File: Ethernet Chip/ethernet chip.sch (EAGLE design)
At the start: 32 parts

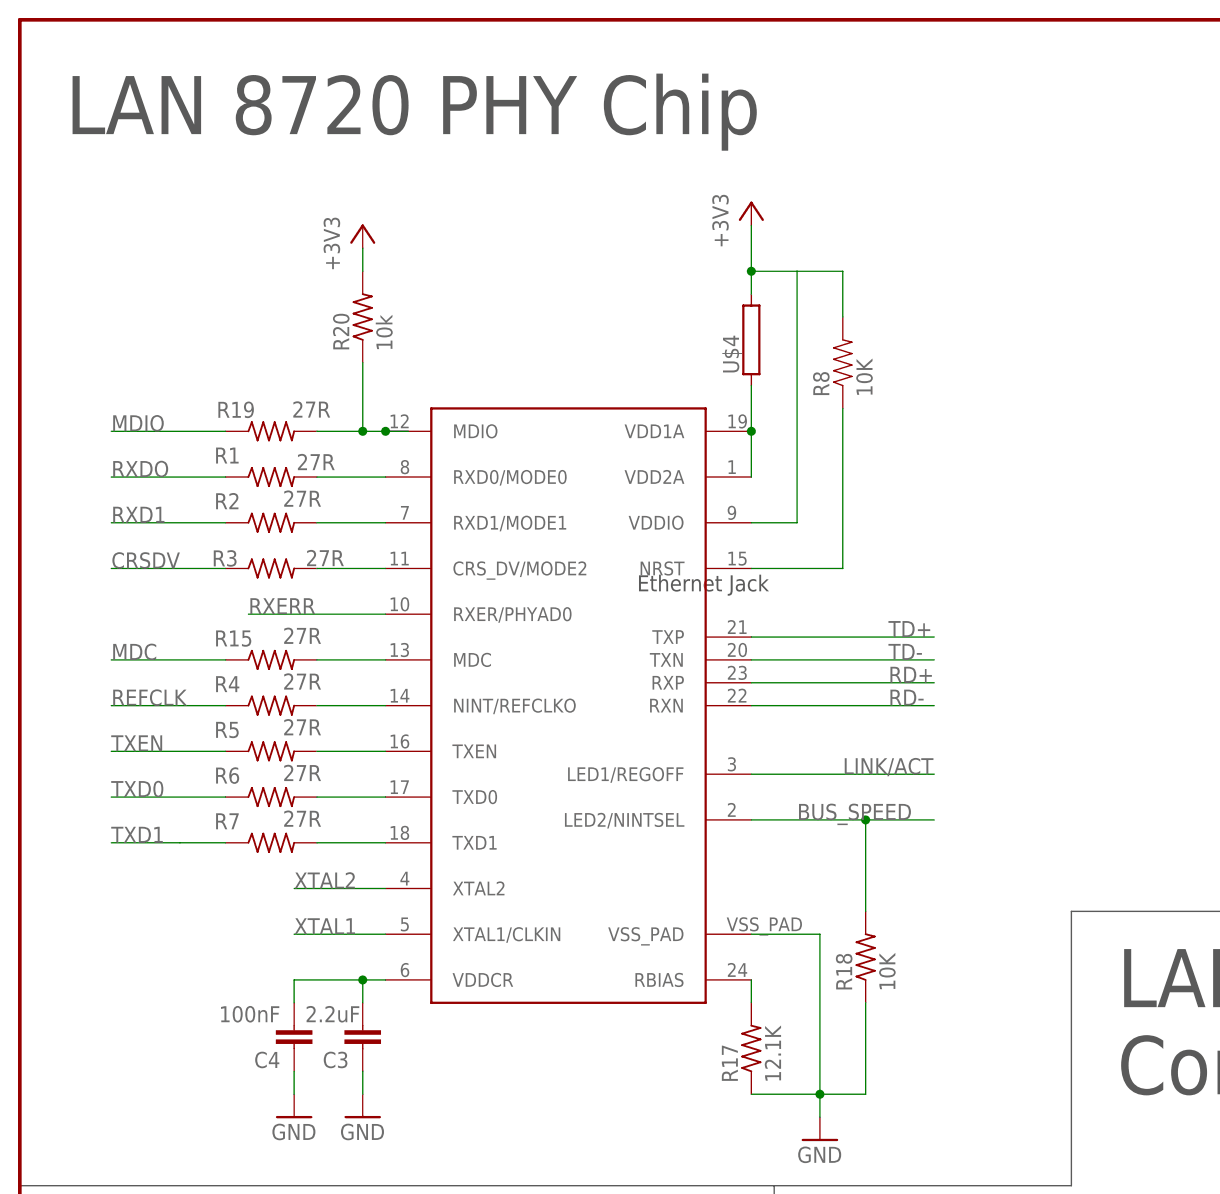
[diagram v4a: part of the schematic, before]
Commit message: Cleaned up the lan8720 schematic
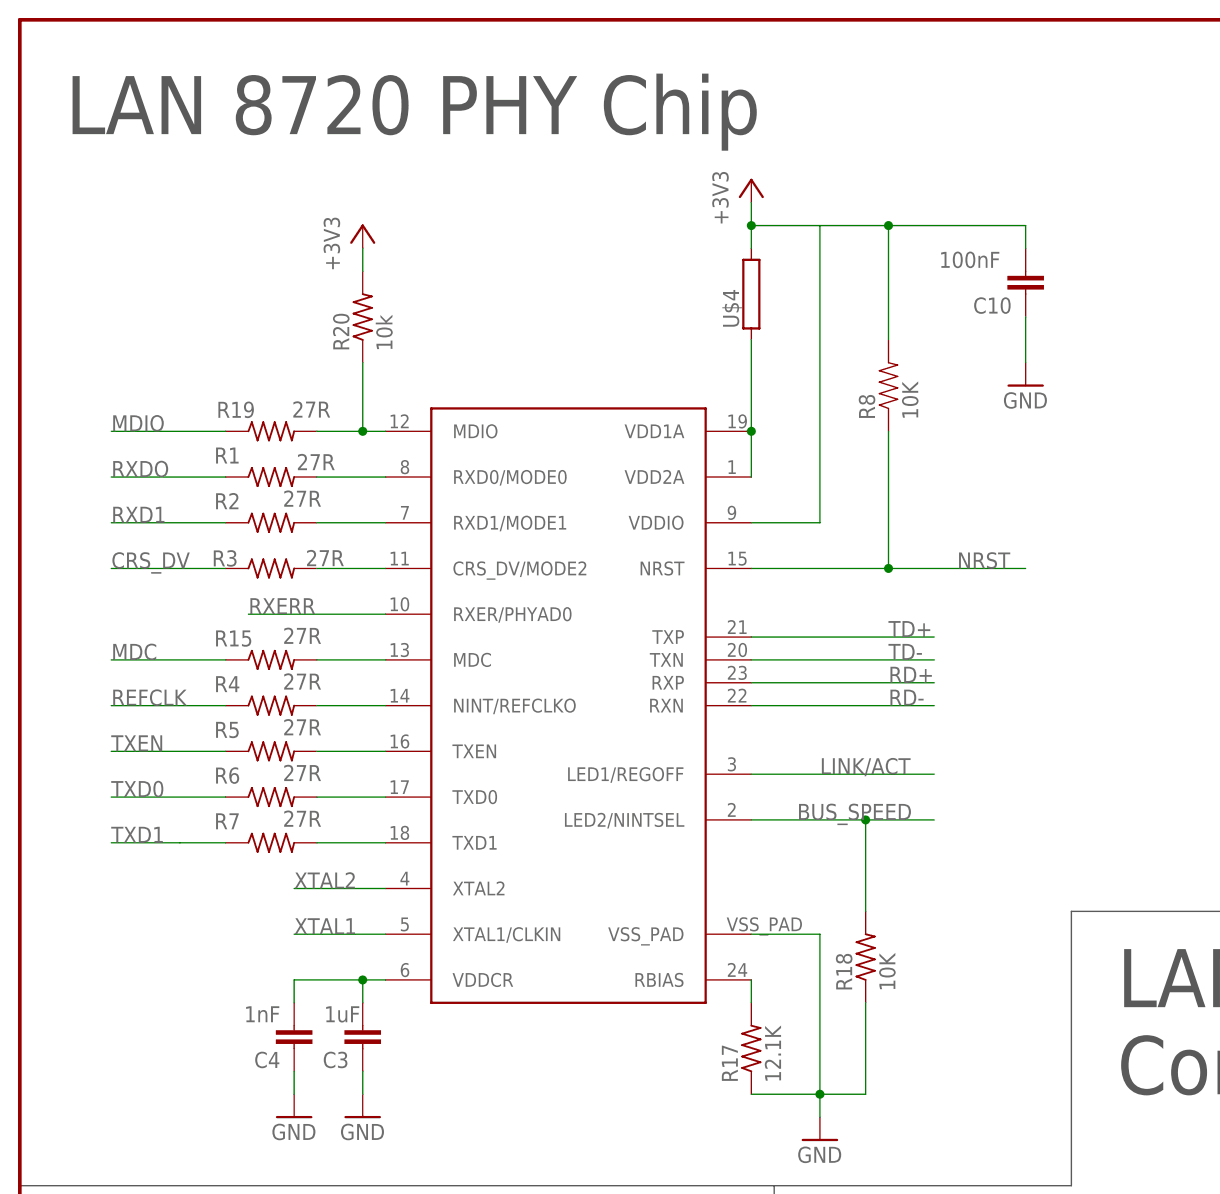
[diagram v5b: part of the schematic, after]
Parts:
- added C10: 100nF, eagle-ltspice:CC0603
- C3: value 2.2uF -> 1uF
- C4: value 100nF -> 1nF
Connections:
- net N$14 renamed NRST
- removed net CRSDV: R3.1
- net +3V3: now also C10.2
- net CRS_DV: now also R3.1
- net GND: now also C10.1
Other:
- moved on the sheet: R8, U$4
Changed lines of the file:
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@@
 <part name="C1" library="eagle-ltspice" deviceset="C" device="C0603" value="22pF"/>
 <part name="C2" library="eagle-ltspice" deviceset="C" device="C0603" value="22pF"/>
-<part name="C3" library="eagle-ltspice" deviceset="C" device="C0603" value="2.2uF"/>
-<part name="C4" library="eagle-ltspice" deviceset="C" device="C0603" value="100nF"/>
+<part name="C3" library="eagle-ltspice" deviceset="C" device="C0603" value="1uF"/>
+<part name="C4" library="eagle-ltspice" deviceset="C" device="C0603" value="1nF"/>
 <part name="C5" library="eagle-ltspice" deviceset="C" device="C0603" value="100nF"/>
 <part name="C6" library="eagle-ltspice" deviceset="C" device="C0603" value="100nF"/>
@@
 <part name="+3V5" library="supply1" deviceset="+3V3" device=""/>
 <part name="+3V6" library="supply1" deviceset="+3V3" device=""/>
+<part name="C10" library="eagle-ltspice" deviceset="C" device="C0603" value="100nF"/>
+<part name="GND8" library="SparkFun-Aesthetics" deviceset="GND" device=""/>
 </parts>
 <sheets>
@@
 <wire x1="15.24" y1="88.9" x2="15.24" y2="-10.16" width="0.1524" layer="97"/>
 <wire x1="15.24" y1="-10.16" x2="121.92" y2="-10.16" width="0.1524" layer="97"/>
-<text x="-58.42" y="25.4" size="1.778" layer="97">Ethernet Jack</text>
 <text x="40.64" y="76.2" size="6.4516" layer="97">Ethernet Jack</text>
 <text x="-121.92" y="76.2" size="6.4516" layer="97">LAN 8720 PHY Chip</text>
@@
 <instance part="GND10" gate="1" x="-38.1" y="-35.56"/>
 <instance part="+3V1" gate="G$1" x="78.74" y="71.12"/>
-<instance part="+3V3" gate="G$1" x="-45.72" y="68.58"/>
+<instance part="+3V3" gate="G$1" x="-45.72" y="71.12"/>
 <instance part="+3V4" gate="G$1" x="30.48" y="30.48"/>
 <instance part="U$1" gate="G$1" x="-66.04" y="12.7"/>
-<instance part="R8" gate="G$1" x="-35.56" y="50.8" rot="R90"/>
+<instance part="R8" gate="G$1" x="-30.48" y="48.26" rot="R90"/>
 <instance part="R1" gate="G$1" x="-99.06" y="38.1" smashed="yes">
 <attribute name="NAME" x="-105.41" y="39.5986" size="1.778" layer="95"/>
@@
 <instance part="U$2" gate="G$1" x="78.74" y="22.86"/>
 <instance part="U$3" gate="G$1" x="-88.9" y="-76.2"/>
-<instance part="U$4" gate="G$1" x="-45.72" y="53.34" rot="R90"/>
+<instance part="U$4" gate="G$1" x="-45.72" y="58.42" rot="R90"/>
 <instance part="R15" gate="G$1" x="-99.06" y="17.78" smashed="yes">
 <attribute name="NAME" x="-105.41" y="19.2786" size="1.778" layer="95"/>
@@
 <instance part="+3V5" gate="G$1" x="58.42" y="-45.72"/>
 <instance part="+3V6" gate="G$1" x="93.98" y="-45.72"/>
+<instance part="C10" gate="G$1" x="-15.24" y="58.42" smashed="yes" rot="R180">
+<attribute name="NAME" x="-16.764" y="58.039" size="1.778" layer="95" rot="R180"/>
+<attribute name="VALUE" x="-18.034" y="63.119" size="1.778" layer="96" rot="R180"/>
+</instance>
+<instance part="GND8" gate="1" x="-15.24" y="48.26"/>
 </instances>
 <busses>
@@
 <wire x1="101.6" y1="-43.18" x2="101.6" y2="-50.8" width="0.1524" layer="91"/>
 </segment>
+<segment>
+<pinref part="C10" gate="G$1" pin="1"/>
+<pinref part="GND8" gate="1" pin="GND"/>
+<wire x1="-15.24" y1="50.8" x2="-15.24" y2="55.88" width="0.1524" layer="91"/>
+</segment>
 </net>
 <net name="+3V3" class="0">
 <segment>
-<wire x1="-45.72" y1="58.42" x2="-45.72" y2="60.96" width="0.1524" layer="91"/>
+<wire x1="-45.72" y1="63.5" x2="-45.72" y2="66.04" width="0.1524" layer="91"/>
 <pinref part="+3V3" gate="G$1" pin="+3V3"/>
 <pinref part="U$4" gate="G$1" pin="2"/>
 <pinref part="U$1" gate="G$1" pin="VDDIO"/>
-<wire x1="-40.64" y1="33.02" x2="-45.72" y2="33.02" width="0.1524" layer="91"/>
-<wire x1="-40.64" y1="33.02" x2="-40.64" y2="60.96" width="0.1524" layer="91"/>
-<junction x="-45.72" y="60.96"/>
+<wire x1="-38.1" y1="33.02" x2="-45.72" y2="33.02" width="0.1524" layer="91"/>
+<wire x1="-38.1" y1="33.02" x2="-38.1" y2="66.04" width="0.1524" layer="91"/>
+<junction x="-45.72" y="66.04"/>
 <pinref part="R8" gate="G$1" pin="2"/>
-<wire x1="-40.64" y1="60.96" x2="-45.72" y2="60.96" width="0.1524" layer="91"/>
-<wire x1="-35.56" y1="55.88" x2="-35.56" y2="60.96" width="0.1524" layer="91"/>
-<wire x1="-35.56" y1="60.96" x2="-40.64" y2="60.96" width="0.1524" layer="91"/>
-<wire x1="-45.72" y1="60.96" x2="-45.72" y2="66.04" width="0.1524" layer="91"/>
+<wire x1="-38.1" y1="66.04" x2="-45.72" y2="66.04" width="0.1524" layer="91"/>
+<wire x1="-30.48" y1="53.34" x2="-30.48" y2="66.04" width="0.1524" layer="91"/>
+<wire x1="-30.48" y1="66.04" x2="-38.1" y2="66.04" width="0.1524" layer="91"/>
+<wire x1="-45.72" y1="66.04" x2="-45.72" y2="68.58" width="0.1524" layer="91"/>
+<pinref part="C10" gate="G$1" pin="2"/>
+<wire x1="-30.48" y1="66.04" x2="-15.24" y2="66.04" width="0.1524" layer="91"/>
+<wire x1="-15.24" y1="66.04" x2="-15.24" y2="63.5" width="0.1524" layer="91"/>
+<junction x="-30.48" y="66.04"/>
 </segment>
 <segment>
@@
 <segment>
 <pinref part="U$1" gate="G$1" pin="VDD1A"/>
-<wire x1="-45.72" y1="43.18" x2="-45.72" y2="48.26" width="0.1524" layer="91"/>
+<wire x1="-45.72" y1="43.18" x2="-45.72" y2="53.34" width="0.1524" layer="91"/>
 <pinref part="U$1" gate="G$1" pin="VDD2A"/>
 <wire x1="-45.72" y1="38.1" x2="-45.72" y2="43.18" width="0.1524" layer="91"/>
@@
 <pinref part="U$1" gate="G$1" pin="LED1/REGOFF"/>
 <wire x1="-45.72" y1="5.08" x2="-25.4" y2="5.08" width="0.1524" layer="91"/>
-<label x="-35.56" y="5.08" size="1.778" layer="95"/>
+<label x="-38.1" y="5.08" size="1.778" layer="95"/>
 </segment>
 </net>
@@
 </segment>
 </net>
-<net name="N$14" class="0">
+<net name="NRST" class="0">
 <segment>
 <pinref part="U$1" gate="G$1" pin="NRST"/>
-<wire x1="-45.72" y1="27.94" x2="-35.56" y2="27.94" width="0.1524" layer="91"/>
-<wire x1="-35.56" y1="27.94" x2="-35.56" y2="45.72" width="0.1524" layer="91"/>
+<wire x1="-45.72" y1="27.94" x2="-30.48" y2="27.94" width="0.1524" layer="91"/>
+<wire x1="-30.48" y1="27.94" x2="-30.48" y2="43.18" width="0.1524" layer="91"/>
 <pinref part="R8" gate="G$1" pin="1"/>
+<wire x1="-30.48" y1="27.94" x2="-15.24" y2="27.94" width="0.1524" layer="91"/>
+<junction x="-30.48" y="27.94"/>
+<label x="-22.86" y="27.94" size="1.778" layer="95"/>
 </segment>
 </net>
@@
 <wire x1="83.82" y1="-38.1" x2="96.52" y2="-38.1" width="0.1524" layer="91"/>
 <label x="86.36" y="-38.1" size="1.778" layer="95"/>
-</segment>
-</net>
-<net name="CRSDV" class="0">
-<segment>
-<wire x1="-104.14" y1="27.94" x2="-116.84" y2="27.94" width="0.1524" layer="91"/>
-<label x="-116.84" y="27.94" size="1.778" layer="95"/>
-<pinref part="R3" gate="G$1" pin="1"/>
 </segment>
 </net>
@@
 <pinref part="R20" gate="G$1" pin="1"/>
 <wire x1="-88.9" y1="43.18" x2="-86.36" y2="43.18" width="0.1524" layer="91"/>
-<wire x1="-86.36" y1="43.18" x2="-83.82" y2="43.18" width="0.1524" layer="91"/>
 <wire x1="-88.9" y1="50.8" x2="-88.9" y2="43.18" width="0.1524" layer="91"/>
 <junction x="-88.9" y="43.18"/>
 <pinref part="U$1" gate="G$1" pin="MDIO"/>
-<junction x="-86.36" y="43.18"/>
 </segment>
 </net>
@@
 <label x="58.42" y="-38.1" size="1.778" layer="95"/>
 </segment>
-</net>
+<segment>
+<wire x1="-104.14" y1="27.94" x2="-116.84" y2="27.94" width="0.1524" layer="91"/>
+<label x="-116.84" y="27.94" size="1.778" layer="95"/>
+<pinref part="R3" gate="G$1" pin="1"/>
+</segment>
+</net>
